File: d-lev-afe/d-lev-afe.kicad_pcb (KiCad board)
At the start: 2 copper layers, 109.4 x 93 mm, 26 parts, among them J1 Conn_01x08, Q1 MMBT3904, Q2 MMBT3906, U1 74AHC04, U2 HT7533-1-SOT89, U3 SRV05-4

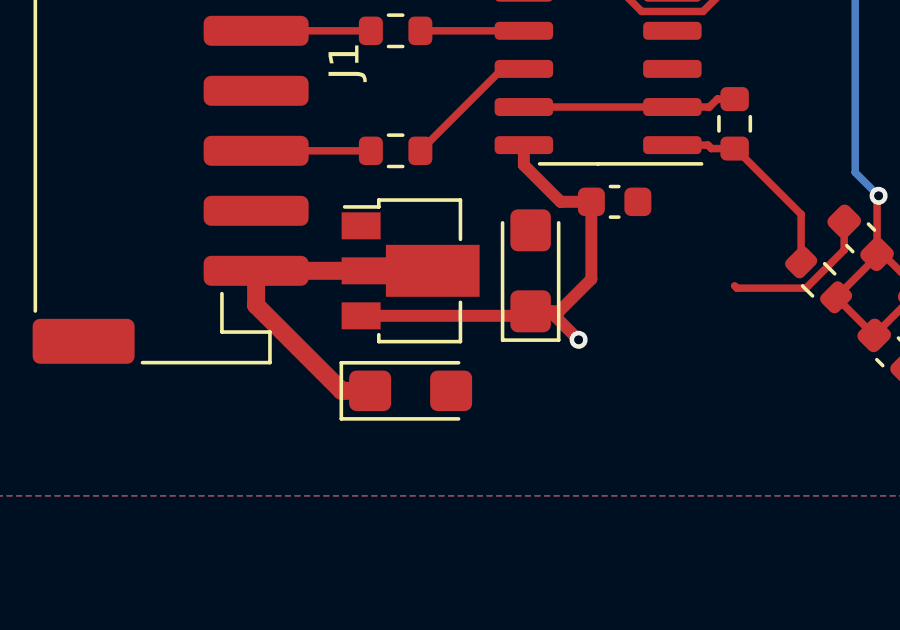
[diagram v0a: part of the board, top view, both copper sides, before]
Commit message: clean up 3d models
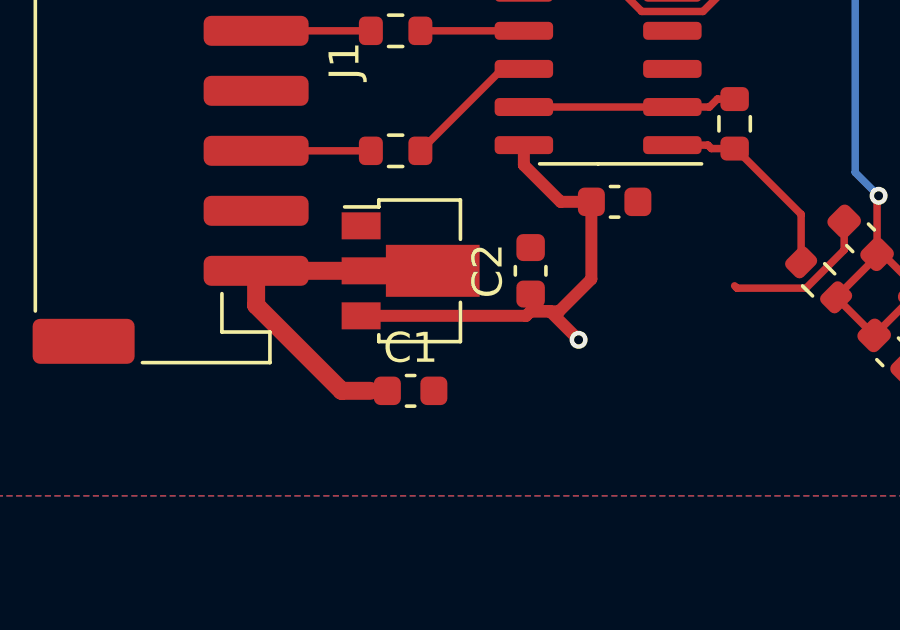
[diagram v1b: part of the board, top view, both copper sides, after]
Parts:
- C1, C2: footprint Capacitor_Tantalum_SMD:CP_EIA-3216-18_Kemet-A -> Capacitor_SMD:C_0603_1608Metric
- J1: value Conn_01x08 -> S8B-PH-SM4-TB

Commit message: many many changes'
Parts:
- removed C8: 1p, Capacitor_SMD:C_0805_2012Metric_Pad1.18x1.45mm_HandSolder
- removed G***: LOGO, theremin:logo
- added AE1: PLATE, theremin:keystone-PN5331TR, F.Cu at (181.3, 107.5)
- added AE2: PLATE, theremin:keystone-PN5331TR, F.Cu at (181.3, 82.5)
- added H4: Standoff_2, theremin:SMTSO-M4, F.Cu at (212.0, 70.0)
- added H5: Standoff_2, theremin:SMTSO-M4, F.Cu at (212.0, 120.0)
- C6: footprint Capacitor_SMD:C_0603_1608Metric -> theremin:testpoint_cap_1pf
- H1, H2, H3, L1: moved to F.Cu
- J1: footprint Connector_JST:JST_PH_S8B-PH-SM4-TB_1x08-1MP_P2.00mm_Horizontal -> theremin:JST_PH_S8B-PH-SM4-TB_1x08-1MP_P2.00mm_Horizontal
- moved H3 78.8 mm to (143.0, 120.0), turned to 0 degrees
- moved C6 45.7 mm to (194.1, 113.0), turned to 180 degrees
- moved H2 44.5 mm to (143.0, 70.0), turned to 0 degrees
- moved L1 32.9 mm to (198.4, 95.0)
- moved C5 25.9 mm to (160.0, 103.1), turned to 90 degrees
- moved U3 23.3 mm to (169.3, 95.1), turned to 90 degrees
- moved R3 23.0 mm to (165.9, 92.7), turned to 180 degrees
- moved C2 22.3 mm to (158.3, 103.1)
- moved U2 22.3 mm to (154.3, 103.1)
- moved C3 21.5 mm to (161.1, 99.7)
- moved J1 21.5 mm to (146.3, 95.0)
- moved R1 21.5 mm to (153.8, 94.0)
- moved R4 21.5 mm to (153.8, 90.0)
- moved R6 21.5 mm to (165.1, 97.1)
- moved R7 21.5 mm to (153.8, 98.0)
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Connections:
- U3 pad 3: L_OUT -> /C_DIV
- U3 pad 4: /C_DIV -> L_OUT
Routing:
- net L_OUT: track 51.2 -> 89.1 mm, vias 0 -> 1
- net GND: track 8.54 -> 42.3 mm, vias 0 -> 14
- net /C_DIV: track 19.4 -> 40.1 mm, vias 2 -> 1
- net L_IN: track 17.9 -> 4.40 mm
- net +3V3: track 24.3 -> 12.8 mm, vias 4 -> 15
- net Net-(R3-Pad2): track 9.78 -> 2.04 mm
- net Net-(R2-Pad1): track 12.5 -> 8.73 mm, vias 0 -> 2
- net Net-(R5-Pad2): track 6.85 -> 3.70 mm
- net +5V: track 9.72 -> 7.20 mm
- net Net-(Q1-B): track 8.97 -> 7.62 mm
- net Net-(R7-Pad1): track 4.58 -> 5.22 mm
- added copper zone on F.Cu, net +3V3
- added copper zone on In2.Cu, net +3V3
- added copper zone on In1.Cu, net GND
- removed copper zone on B.Cu, net +3V3
- removed copper zone on F.Cu, net GND
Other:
- board size 109.4 x 93 mm -> 90.6 x 73.2 mm
- copper layers 2 -> 4
- rule solder_mask_min_width: 0.2 -> 0.15
- board text removed: "L_OUT Drive side - near antenna mount"
- board text removed: "Sense side Minimize copper"

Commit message: many more changes
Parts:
- removed U2: HT7533-1-SOT89, Package_TO_SOT_SMD:SOT-89-3
- added U4: AP2112K-3.3, Package_TO_SOT_SMD:SOT-23-5, F.Cu at (153.8, 103.1)
- moved C3 2.40 mm to (158.7, 99.7)
- moved C5 2.35 mm to (157.6, 103.3), turned to 0 degrees
- moved C2 1.64 mm to (157.6, 101.6), turned to 0 degrees
- moved C1 0.89 mm to (153.4, 100.5), turned to 0 degrees
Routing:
- net +3V3: track 12.8 -> 7.40 mm, vias 15 -> 7
- net +5V: track 7.20 -> 12.0 mm
- net GND: track 42.3 -> 42.9 mm, vias 14 -> 15

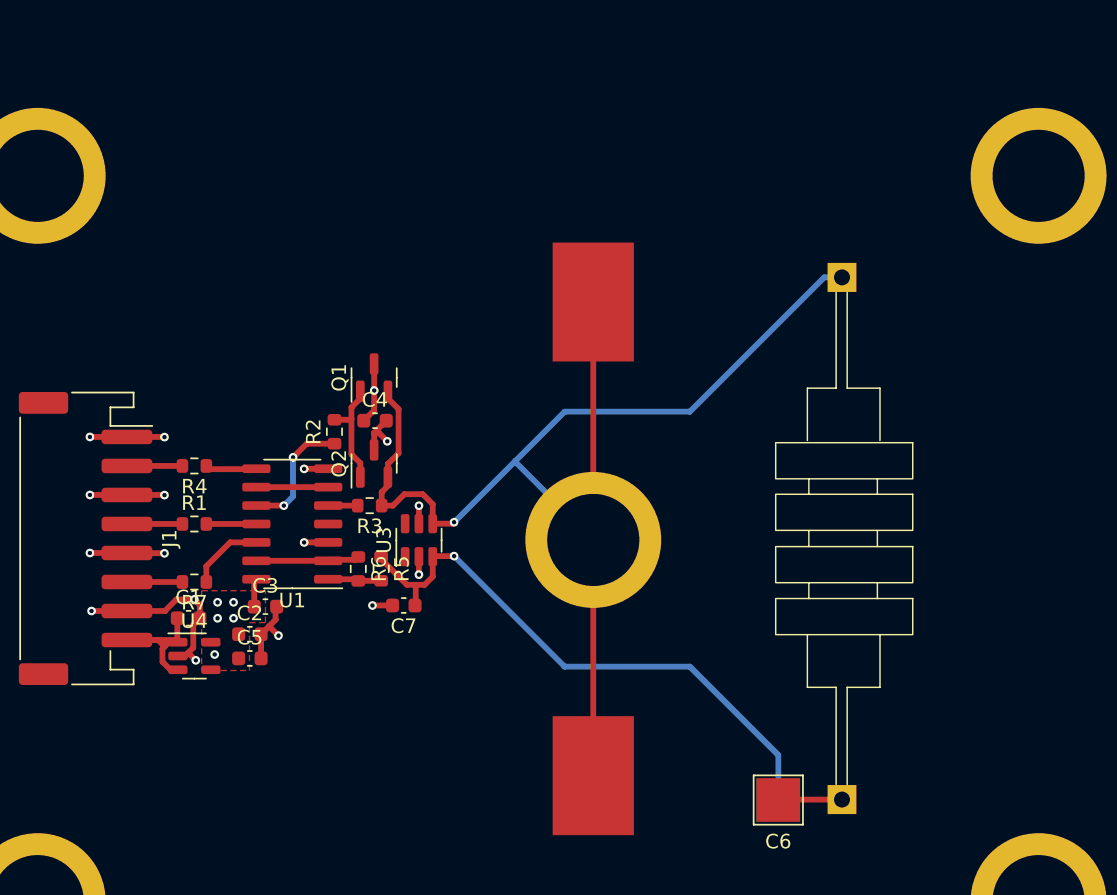
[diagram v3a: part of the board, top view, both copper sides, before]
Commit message: Aesthetic improvements to main/AFE
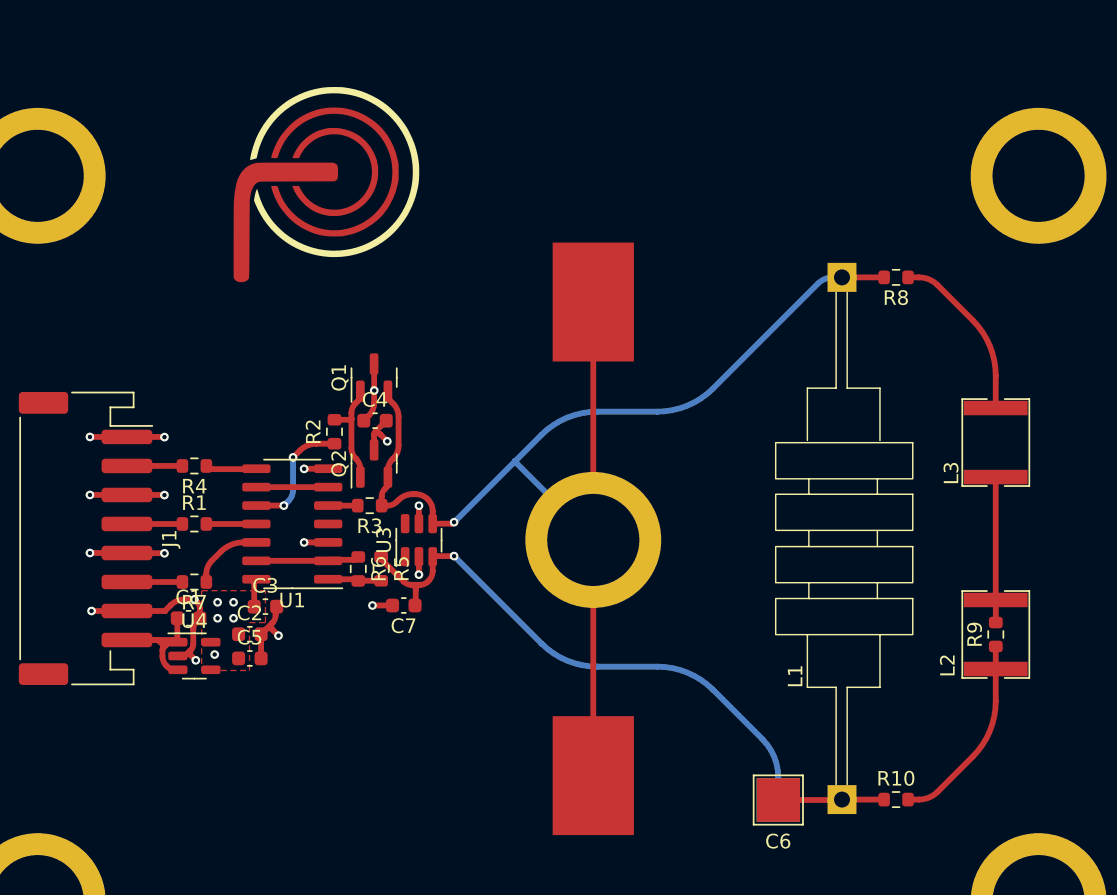
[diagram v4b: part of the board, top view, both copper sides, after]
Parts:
- added G***: LOGO, theremin:logo, F.Cu at (163.7, 69.7)
- added L2: 1m, theremin:Coilcraft_DO1605T, F.Cu at (209.1, 101.6)
- added L3: 1m, theremin:Coilcraft_DO1605T, F.Cu at (209.1, 88.4)
- added R10: 0, Resistor_SMD:R_0603_1608Metric, F.Cu at (202.2, 113.0)
- added R8: 0, Resistor_SMD:R_0603_1608Metric, F.Cu at (202.2, 77.0)
- added R9: 0, Resistor_SMD:R_0603_1608Metric, F.Cu at (209.1, 101.6)
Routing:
- net Net-(L2-Pad1): track 0.00 -> 13.6 mm
- net Net-(L3-Pad2): track 0.00 -> 12.0 mm
- net Net-(L2-Pad2): track 0.00 -> 10.0 mm
- net L_IN: track 4.40 -> 7.30 mm
- net L_OUT: track 89.1 -> 91.0 mm
- net GND: track 42.9 -> 43.8 mm

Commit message: more aesthetics
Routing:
- added copper zone on In1.Cu, net (none)

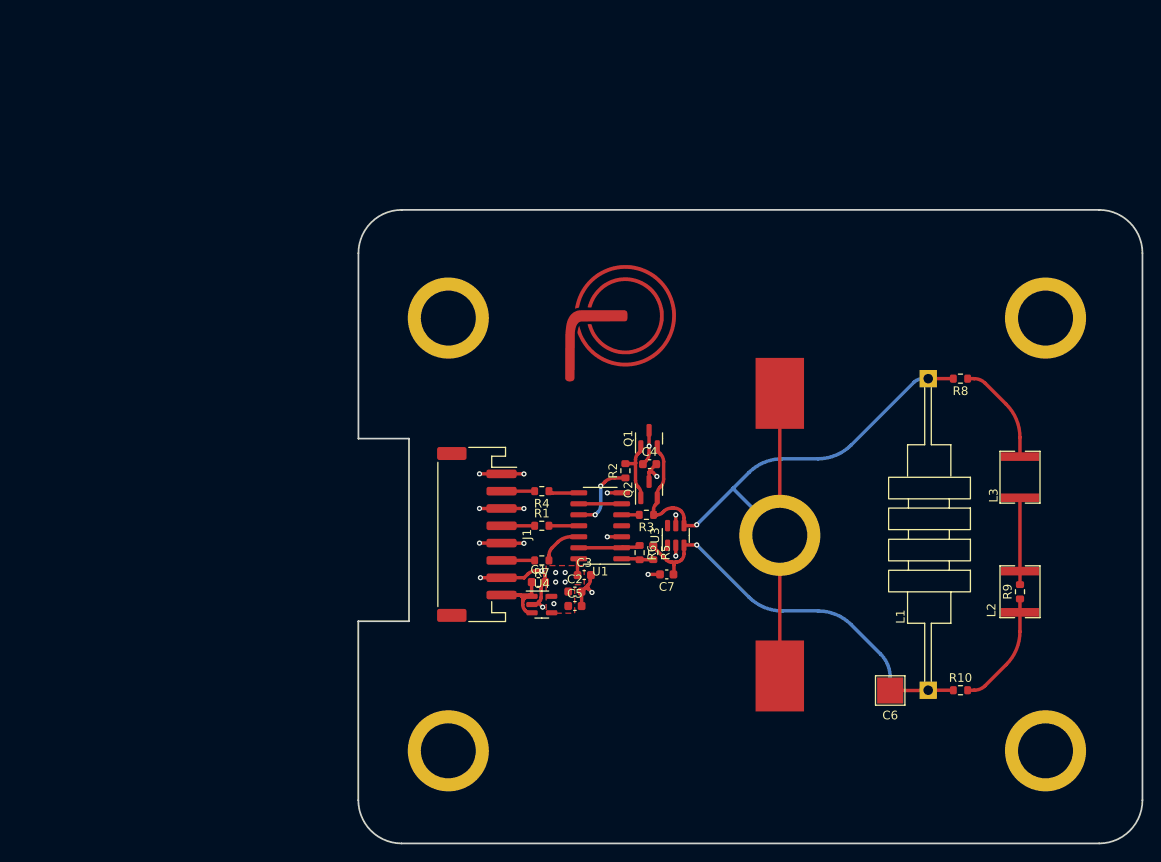
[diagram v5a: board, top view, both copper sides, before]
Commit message: d-lev-afe: de-rounded traces
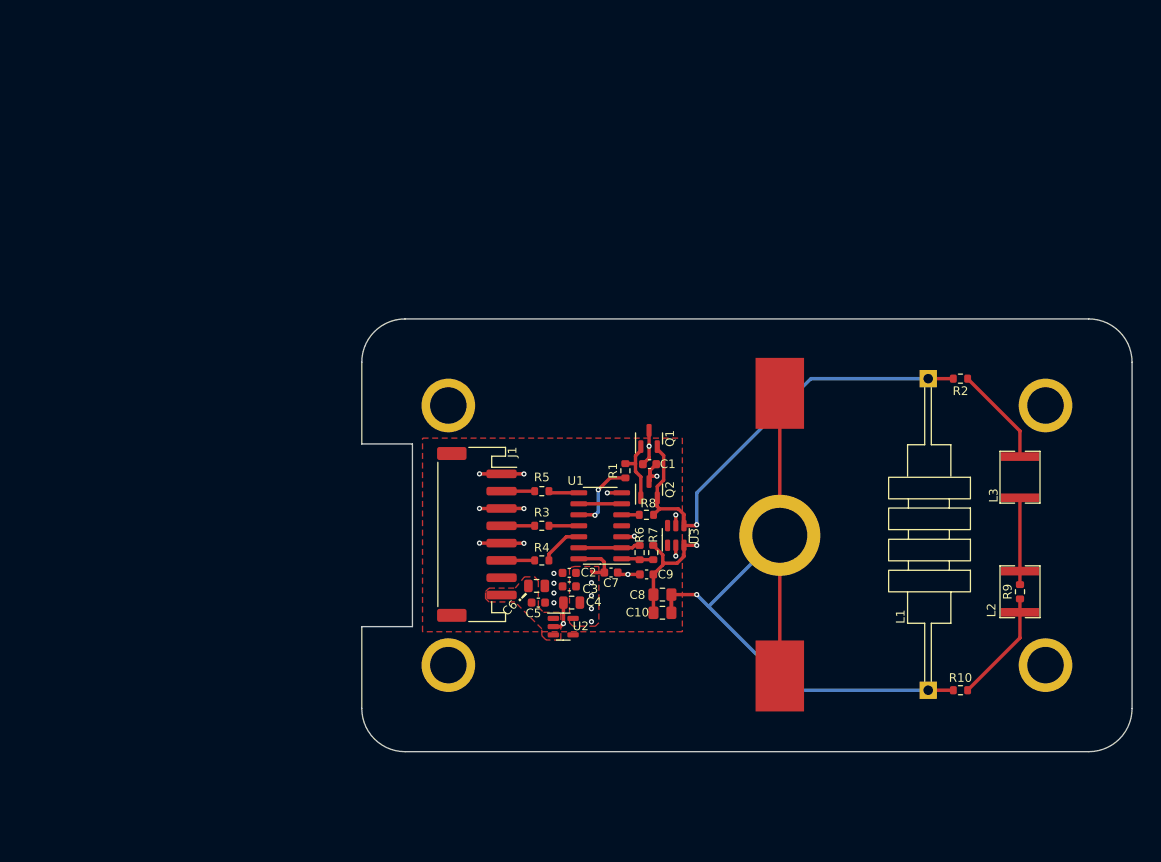
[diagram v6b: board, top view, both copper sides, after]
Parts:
- removed the C1 at (153.4, 100.5)
- removed G***: LOGO, theremin:logo
- removed U4: AP2112K-3.3, Package_TO_SOT_SMD:SOT-23-5
- added C10: 1p, Capacitor_SMD:C_0805_2012Metric_Pad1.18x1.45mm_HandSolder, F.Cu at (167.7, 104.0)
- added C3: 1u, Capacitor_SMD:C_0603_1608Metric, F.Cu at (157.0, 101.0)
- added C4: 10u, Capacitor_SMD:C_0805_2012Metric, F.Cu at (157.3, 102.9)
- added C6: 10u, Capacitor_SMD:C_0805_2012Metric, F.Cu at (153.2, 100.9)
- added U2: AP2112K-3.3, Package_TO_SOT_SMD:SOT-23-5, F.Cu at (156.3, 105.6)
- C2: value 10uF -> .1u
- C5: value 0.1uF -> 1u
- C8: renamed from C6; footprint theremin:testpoint_cap_1pf -> Capacitor_SMD:C_0805_2012Metric_Pad1.18x1.45mm_HandSolder
- H1: renamed from H2; footprint theremin:SMTSO-M4 -> theremin:SMTSO-M3
- H2: renamed from H4; footprint theremin:SMTSO-M4 -> theremin:SMTSO-M3
- H3, H5: footprint theremin:SMTSO-M4 -> theremin:SMTSO-M3
- moved C8 28.6 mm to (167.7, 102.0)
- moved H1 10.1 mm to (143.0, 80.1)
- moved H2 10.1 mm to (212.0, 80.1)
- moved H3 9.90 mm to (143.0, 110.1)
- moved H5 9.90 mm to (212.0, 110.1)
- moved C5 4.24 mm to (153.4, 102.9), turned to 180 degrees
- moved C7 3.11 mm to (161.8, 99.4)
- moved C9 2.33 mm to (165.9, 99.6)
- moved C2 2.26 mm to (157.0, 99.4)
- renumbered AE2 to AE1, AE1 to AE2, C4 to C1, C3 to C7, C7 to C9, H1 to H4, R2 to R1, R8 to R2, R1 to R3, R7 to R4, R4 to R5, R5 to R7, R3 to R8
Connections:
- AE1 pad 1: L_OUT -> L_IN
- AE2 pad 1: L_OUT -> L_IN
- C2 pad 1: +3V3 -> GND
- C2 pad 2: GND -> +3V3
- C5 pad 1: +3V3 -> GND
- C5 pad 2: GND -> +5V
- H4 pad 1: L_OUT -> L_IN
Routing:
- net L_IN: track 7.30 -> 85.7 mm, vias 0 -> 1
- net L_OUT: track 91.0 -> 53.6 mm
- net /C_DIV: track 39.9 -> 14.3 mm
- net GND: track 43.8 -> 29.9 mm, vias 15 -> 16
- net +5V: track 12.1 -> 0.00 mm
- net +3V3: track 7.33 -> 11.3 mm, vias 7 -> 6
- net Net-(L2-Pad1): track 13.6 -> 13.1 mm
- net Net-(L3-Pad2): track 12.0 -> 11.5 mm
- added copper zone on F.Cu, net +5V
- added copper zone on F.Cu, net GND
- removed copper zone on In1.Cu, net (none)
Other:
- board size 90.6 x 73.2 mm -> 89 x 50 mm
- board text added: "!"
